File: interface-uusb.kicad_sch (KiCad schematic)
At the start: 1 part, among them J1 USB_B_Micro

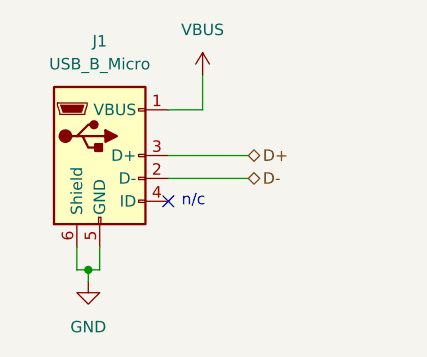
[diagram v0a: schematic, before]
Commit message: Adding symbols information
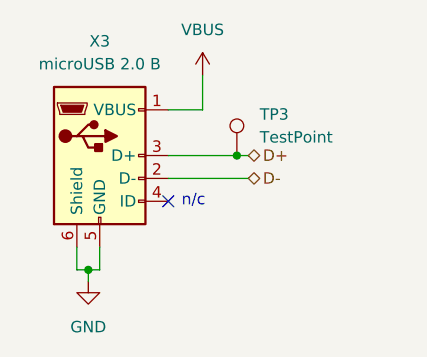
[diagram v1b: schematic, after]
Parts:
- added TP3: TestPoint, symbol Connector:TestPoint
- X3: renamed from J1; value USB_B_Micro -> microUSB 2.0 B; footprint (none) -> Connector_USB:USB_Micro-B_Amphenol_10118194_Horizontal; Mfr (none) -> Amphenol ICC (FCI); Mfr P/N (none) -> 10118194-0001LF; Supplier_1 (none) -> Digikey; Supplier_1 P/N (none) -> 609-4618-1-ND; Supplier_1 Price @ Qty (none) -> 0.32930; Supplier_1 Unit Price (none) -> 0.57
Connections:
- net D+: now also TP3.1
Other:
- company: (none) -> catbranchman
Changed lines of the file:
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@@
 	(generator_version "8.0")
 	(paper "A4")
+	(title_block
+		(company "catbranchman")
+		(comment 1 "Electrical Engineering Department")
+		(comment 2 "EE 156 / Stanford University")
+		(comment 3 "Flight Club, W6YX, Endurance")
+	)
 	(junction
 		(at 140.97 111.76)
@@
 		(color 0 0 0 0)
 	)
+	(junction
+		(at 157.48 99.06)
+		(diameter 0)
+		(color 0 0 0 0)
+	)
 	(no_connect
 		(at 149.86 104.14)
@@
 	(wire
 		(pts
+			(xy 157.48 99.06) (xy 158.75 99.06)
+		)
+		(stroke
+			(width 0)
+			(type default)
+		)
+	)
+	(wire
+		(pts
 			(xy 139.7 111.76) (xy 140.97 111.76)
 		)
@@
 	(wire
 		(pts
-			(xy 149.86 99.06) (xy 158.75 99.06)
+			(xy 149.86 99.06) (xy 157.48 99.06)
 		)
 		(stroke
@@
 		(dnp no)
 		(fields_autoplaced yes)
-		(property "Reference" "J1"
+		(property "Reference" "X3"
 			(at 142.24 86.36 0)
 			(effects
@@
 			)
 		)
-		(property "Value" "USB_B_Micro"
+		(property "Value" "microUSB 2.0 B"
 			(at 142.24 88.9 0)
 			(effects
@@
 			)
 		)
-		(property "Footprint" ""
+		(property "Footprint" "Connector_USB:USB_Micro-B_Amphenol_10118194_Horizontal"
 			(at 146.05 100.33 0)
 			(effects
@@
 			)
 		)
-		(property "Datasheet" "~"
+		(property "Datasheet" "https://cdn.amphenol-cs.com/media/wysiwyg/files/documentation/datasheet/inputoutput/io_usb_micro.pdf"
 			(at 146.05 100.33 0)
 			(effects
@@
 			)
 		)
-		(property "Description" "USB Micro Type B connector"
+		(property "Description" "USB - micro B USB 2.0 Receptacle Connector 5 Position Surface Mount, Right Angle."
+			(at 142.24 99.06 0)
+			(effects
+				(font
+					(size 1.27 1.27)
+				)
+				(hide yes)
+			)
+		)
+		(property "Mfr" "Amphenol ICC (FCI)"
+			(at 142.24 99.06 0)
+			(effects
+				(font
+					(size 1.27 1.27)
+				)
+				(hide yes)
+			)
+		)
+		(property "Mfr P/N" "10118194-0001LF"
+			(at 142.24 99.06 0)
+			(effects
+				(font
+					(size 1.27 1.27)
+				)
+				(hide yes)
+			)
+		)
+		(property "Supplier_1" "Digikey"
+			(at 142.24 99.06 0)
+			(effects
+				(font
+					(size 1.27 1.27)
+				)
+				(hide yes)
+			)
+		)
+		(property "Supplier_1 P/N" "609-4618-1-ND"
+			(at 142.24 99.06 0)
+			(effects
+				(font
+					(size 1.27 1.27)
+				)
+				(hide yes)
+			)
+		)
+		(property "Supplier_1 Unit Price" "0.57"
+			(at 142.24 99.06 0)
+			(effects
+				(font
+					(size 1.27 1.27)
+				)
+				(hide yes)
+			)
+		)
+		(property "Supplier_1 Price @ Qty" "0.32930"
+			(at 142.24 99.06 0)
+			(effects
+				(font
+					(size 1.27 1.27)
+				)
+				(hide yes)
+			)
+		)
+		(property "Supplier_2" ""
+			(at 142.24 99.06 0)
+			(effects
+				(font
+					(size 1.27 1.27)
+				)
+				(hide yes)
+			)
+		)
+		(property "Supplier_2 P/N" ""
+			(at 142.24 99.06 0)
+			(effects
+				(font
+					(size 1.27 1.27)
+				)
+				(hide yes)
+			)
+		)
+		(property "Supplier_2 Unit Price" ""
+			(at 142.24 99.06 0)
+			(effects
+				(font
+					(size 1.27 1.27)
+				)
+				(hide yes)
+			)
+		)
+		(property "Supplier_2 Price @ Qty" ""
 			(at 142.24 99.06 0)
 			(effects
@@
 			(project ""
 				(path "/1c59de6a-87fe-4223-8898-4b0383164a31/e9b3da3a-64c8-4ad5-ba76-a4a7346ea25f"
-					(reference "J1")
+					(reference "X3")
 					(unit 1)
 				)
@@
 					(unit 1)
 				)
+			)
+		)
+	)
+	(symbol
+		(lib_id "Connector:TestPoint")
+		(at 157.48 99.06 0)
+		(unit 1)
+		(exclude_from_sim no)
+		(in_bom yes)
+		(on_board yes)
+		(dnp no)
+		(fields_autoplaced yes)
+		(property "Reference" "TP3"
+			(at 160.02 94.4879 0)
+			(effects
+				(font
+					(size 1.27 1.27)
+				)
+				(justify left)
+			)
+		)
+		(property "Value" "TestPoint"
+			(at 160.02 97.0279 0)
+			(effects
+				(font
+					(size 1.27 1.27)
+				)
+				(justify left)
+			)
+		)
+		(property "Footprint" ""
+			(at 162.56 99.06 0)
+			(effects
+				(font
+					(size 1.27 1.27)
+				)
+				(hide yes)
+			)
+		)
+		(property "Datasheet" "~"
+			(at 162.56 99.06 0)
+			(effects
+				(font
+					(size 1.27 1.27)
+				)
+				(hide yes)
+			)
+		)
+		(property "Description" "test point"
+			(at 157.48 99.06 0)
+			(effects
+				(font
+					(size 1.27 1.27)
+				)
+				(hide yes)
+			)
+		)
+		(pin "1"
+		)
+		(instances
+			(project ""
+				(path "/1c59de6a-87fe-4223-8898-4b0383164a31/e9b3da3a-64c8-4ad5-ba76-a4a7346ea25f"
+					(reference "TP3")
+					(unit 1)
+				)

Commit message: Fixing footprint imports
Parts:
- added TP4: TestPoint, TestPoint:TestPoint_Pad_D1.0mm, symbol Connector:TestPoint
- TP3: footprint (none) -> TestPoint:TestPoint_Pad_D1.0mm
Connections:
- net D-: now also TP4.1

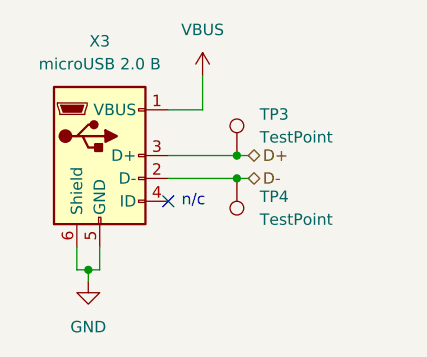
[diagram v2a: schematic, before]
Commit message: Spamming 0 ohm resistors
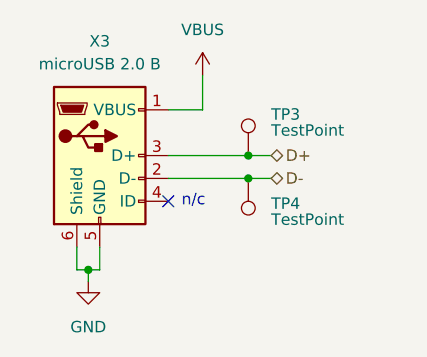
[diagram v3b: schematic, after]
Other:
- title: (none) -> Interface - uUSB
- moved on the sheet: TP3, TP4
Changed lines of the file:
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@@
 	(paper "A4")
 	(title_block
+		(title "Interface - uUSB")
 		(company "catbranchman")
 		(comment 1 "Electrical Engineering Department")
@@
 	)
 	(junction
-		(at 157.48 101.6)
+		(at 158.75 101.6)
 		(diameter 0)
 		(color 0 0 0 0)
@@
 	)
 	(junction
-		(at 157.48 99.06)
+		(at 158.75 99.06)
 		(diameter 0)
 		(color 0 0 0 0)
@@
 	(wire
 		(pts
-			(xy 149.86 101.6) (xy 157.48 101.6)
-		)
-		(stroke
-			(width 0)
-			(type default)
-		)
-	)
-	(wire
-		(pts
-			(xy 157.48 99.06) (xy 158.75 99.06)
-		)
-		(stroke
-			(width 0)
-			(type default)
-		)
-	)
-	(wire
-		(pts
-			(xy 157.48 101.6) (xy 158.75 101.6)
+			(xy 149.86 101.6) (xy 158.75 101.6)
+		)
+		(stroke
+			(width 0)
+			(type default)
+		)
+	)
+	(wire
+		(pts
+			(xy 158.75 101.6) (xy 161.29 101.6)
 		)
 		(stroke
@@
 	(wire
 		(pts
-			(xy 149.86 99.06) (xy 157.48 99.06)
+			(xy 158.75 99.06) (xy 161.29 99.06)
+		)
+		(stroke
+			(width 0)
+			(type default)
+		)
+	)
+	(wire
+		(pts
+			(xy 149.86 99.06) (xy 158.75 99.06)
 		)
 		(stroke
@@
 	(hierarchical_label "D+"
 		(shape bidirectional)
-		(at 158.75 99.06 0)
+		(at 161.29 99.06 0)
 		(fields_autoplaced yes)
 		(effects
@@
 	(hierarchical_label "D-"
 		(shape bidirectional)
-		(at 158.75 101.6 0)
+		(at 161.29 101.6 0)
 		(fields_autoplaced yes)
 		(effects
@@
 	(symbol
 		(lib_id "Connector:TestPoint")
-		(at 157.48 101.6 180)
+		(at 158.75 101.6 180)
 		(unit 1)
 		(exclude_from_sim no)
@@
 		(on_board yes)
 		(dnp no)
-		(fields_autoplaced yes)
 		(property "Reference" "TP4"
-			(at 160.02 103.6319 0)
+			(at 161.29 104.394 0)
 			(effects
 				(font
@@
 		)
 		(property "Value" "TestPoint"
-			(at 160.02 106.1719 0)
+			(at 161.29 106.1719 0)
 			(effects
 				(font
@@
 		)
 		(property "Footprint" "TestPoint:TestPoint_Pad_D1.0mm"
-			(at 152.4 101.6 0)
+			(at 153.67 101.6 0)
 			(effects
 				(font
@@
 		)
 		(property "Datasheet" "~"
-			(at 152.4 101.6 0)
+			(at 153.67 101.6 0)
 			(effects
 				(font
@@
 		)
 		(property "Description" "test point"
-			(at 157.48 101.6 0)
+			(at 158.75 101.6 0)
 			(effects
 				(font
@@
 		)
 		(property "Mfr" ""
-			(at 157.48 101.6 0)
+			(at 158.75 101.6 0)
 			(effects
 				(font
@@
 		)
 		(property "Mfr P/N" ""
-			(at 157.48 101.6 0)
+			(at 158.75 101.6 0)
 			(effects
 				(font
@@
 		)
 		(property "Supplier_1" ""
-			(at 157.48 101.6 0)
+			(at 158.75 101.6 0)
 			(effects
 				(font
@@
 		)
 		(property "Supplier_1 P/N" ""
-			(at 157.48 101.6 0)
+			(at 158.75 101.6 0)
 			(effects
 				(font
@@
 		)
 		(property "Supplier_1 Unit Price" ""
-			(at 157.48 101.6 0)
+			(at 158.75 101.6 0)
 			(effects
 				(font
@@
 		)
 		(property "Supplier_1 Price @ Qty" ""
-			(at 157.48 101.6 0)
+			(at 158.75 101.6 0)
 			(effects
 				(font
@@
 		)
 		(property "Supplier_2" ""
-			(at 157.48 101.6 0)
+			(at 158.75 101.6 0)
 			(effects
 				(font
@@
 		)
 		(property "Supplier_2 P/N" ""
-			(at 157.48 101.6 0)
+			(at 158.75 101.6 0)
 			(effects
 				(font
@@
 		)
 		(property "Supplier_2 Unit Price" ""
-			(at 157.48 101.6 0)
+			(at 158.75 101.6 0)
 			(effects
 				(font
@@
 		)
 		(property "Supplier_2 Price @ Qty" ""
-			(at 157.48 101.6 0)
+			(at 158.75 101.6 0)
 			(effects
 				(font
@@
 	(symbol
 		(lib_id "Connector:TestPoint")
-		(at 157.48 99.06 0)
+		(at 158.75 99.06 0)
 		(unit 1)
 		(exclude_from_sim no)
@@
 		(on_board yes)
 		(dnp no)
-		(fields_autoplaced yes)
 		(property "Reference" "TP3"
-			(at 160.02 94.4879 0)
+			(at 161.29 94.4879 0)
 			(effects
 				(font
@@
 		)
 		(property "Value" "TestPoint"
-			(at 160.02 97.0279 0)
+			(at 161.29 96.266 0)
 			(effects
 				(font
@@
 		)
 		(property "Footprint" "TestPoint:TestPoint_Pad_D1.0mm"
-			(at 162.56 99.06 0)
+			(at 163.83 99.06 0)
 			(effects
 				(font
@@
 		)
 		(property "Datasheet" "~"
-			(at 162.56 99.06 0)
+			(at 163.83 99.06 0)
 			(effects
 				(font
@@
 		)
 		(property "Description" "test point"
-			(at 157.48 99.06 0)
+			(at 158.75 99.06 0)
 			(effects
 				(font
@@
 		)
 		(property "Mfr" ""
-			(at 157.48 99.06 0)
+			(at 158.75 99.06 0)
 			(effects
 				(font
@@
 		)
 		(property "Mfr P/N" ""
-			(at 157.48 99.06 0)
+			(at 158.75 99.06 0)
 			(effects
 				(font
@@
 		)
 		(property "Supplier_1" ""
-			(at 157.48 99.06 0)
+			(at 158.75 99.06 0)
 			(effects
 				(font
@@
 		)
 		(property "Supplier_1 P/N" ""
-			(at 157.48 99.06 0)
+			(at 158.75 99.06 0)
 			(effects
 				(font
@@
 		)
 		(property "Supplier_1 Unit Price" ""
-			(at 157.48 99.06 0)
+			(at 158.75 99.06 0)
 			(effects
 				(font
@@
 		)
 		(property "Supplier_1 Price @ Qty" ""
-			(at 157.48 99.06 0)
+			(at 158.75 99.06 0)
 			(effects
 				(font
@@
 		)
 		(property "Supplier_2" ""
-			(at 157.48 99.06 0)
+			(at 158.75 99.06 0)
 			(effects
 				(font
@@
 		)
 		(property "Supplier_2 P/N" ""
-			(at 157.48 99.06 0)
+			(at 158.75 99.06 0)
 			(effects
 				(font
@@
 		)
 		(property "Supplier_2 Unit Price" ""
-			(at 157.48 99.06 0)
+			(at 158.75 99.06 0)
 			(effects
 				(font
@@
 		)
 		(property "Supplier_2 Price @ Qty" ""
-			(at 157.48 99.06 0)
-			(effects
-				(font
+			(at 158.75 99.06 0)
+			(effects
+				(font

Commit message: Creating fab package
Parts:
- TP3: value TestPoint -> D+ Testpoint
- TP4: value TestPoint -> D- TestPoint
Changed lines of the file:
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@@
 			)
 		)
-		(property "Value" "TestPoint"
+		(property "Value" "D- TestPoint"
 			(at 161.29 106.1719 0)
 			(effects
@@
 			)
 		)
-		(property "Value" "TestPoint"
+		(property "Value" "D+ Testpoint"
 			(at 161.29 96.266 0)
 			(effects
